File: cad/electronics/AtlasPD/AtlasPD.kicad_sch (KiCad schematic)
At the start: 0 parts

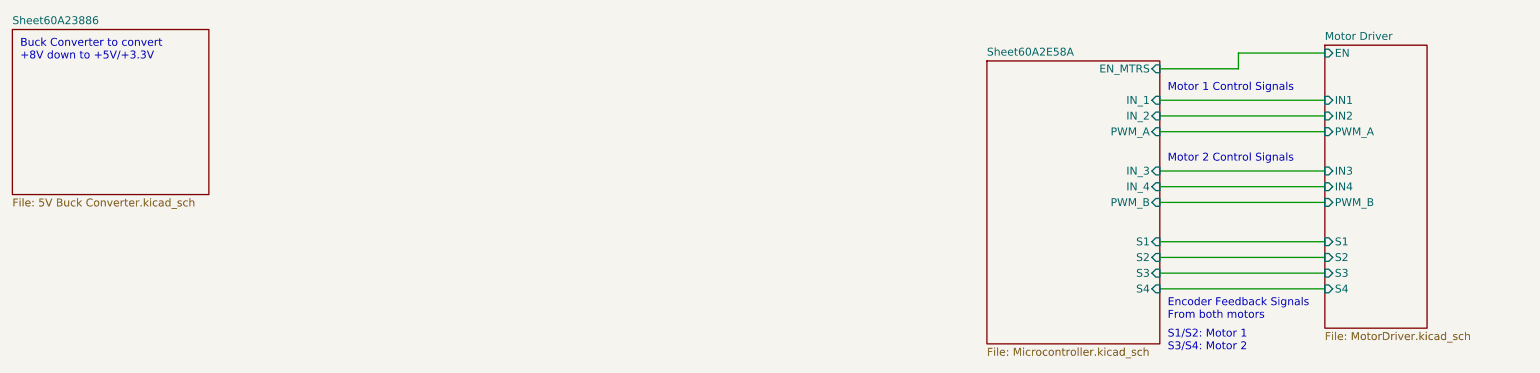
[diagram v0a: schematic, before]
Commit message: Finished IC Schematic, Assigned footprints
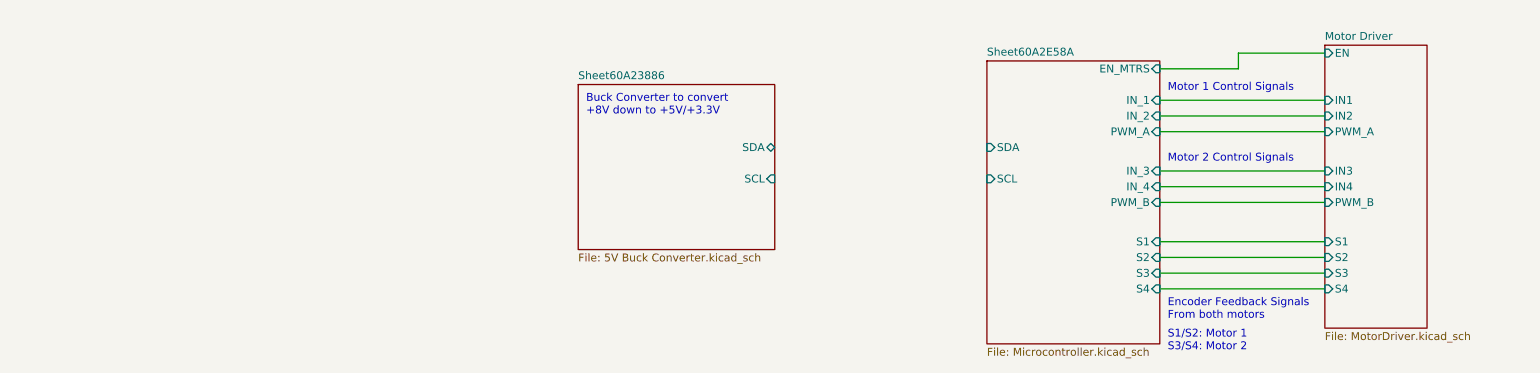
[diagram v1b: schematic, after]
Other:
- sheet Sheet60A23886 ports: added SCL, SDA; removed none
- sheet Sheet60A2E58A ports: added SCL, SDA; removed none

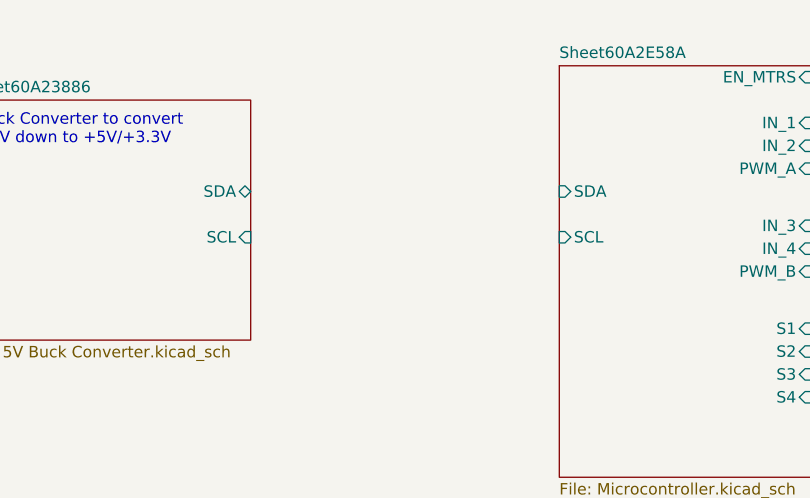
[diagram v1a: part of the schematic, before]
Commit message: Fixed schematic issues from KiCAD upgrade, Moved 3.3V LDO to MCU Sheet
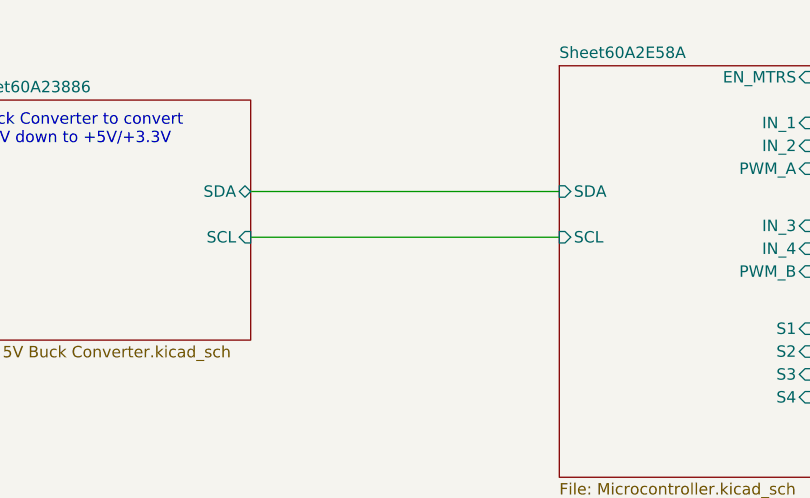
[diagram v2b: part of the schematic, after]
